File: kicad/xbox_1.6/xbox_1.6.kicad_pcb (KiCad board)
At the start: 2 copper layers, 6 parts, among them U2C1 intel_495_bga2, U4B1 ddr_100_tqfp, U4C1 nvidia_xgpu_nv2a, U5F1 ddr_100_tqfp, U6D1 ddr_100_tqfp, U6E1 nvidia_mcpx

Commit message: route more
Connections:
- U2C1 pad A2: (no net) -> /VSS
- U2C1 pad A3: (no net) -> /CPU_A29
- U2C1 pad A4: (no net) -> /CPU_A32
- U2C1 pad A5: (no net) -> /CPU_A33
- U2C1 pad A6: (no net) -> /CPU_RESET
- U2C1 pad A7: (no net) -> /VSS
- U2C1 pad A8: (no net) -> /VSS
- U2C1 pad A9: (no net) -> /CPU_D5
- U2C1 pad B1: (no net) -> /VSS
- U2C1 pad B2: (no net) -> /CPU_A30
- U2C1 pad B3: (no net) -> /CPU_A28
- U2C1 pad B4: (no net) -> /CPU_A34
- U2C1 pad B5: (no net) -> /VSS
- U2C1 pad B6: (no net) -> /VSS
- U2C1 pad B7: (no net) -> /VSS
- U2C1 pad B8: (no net) -> /VSS
- U2C1 pad C1: (no net) -> /CPU_A27
- U2C1 pad C2: (no net) -> /CPU_A31
- U2C1 pad C3: (no net) -> /CPU_A26
- U2C1 pad C4: (no net) -> /CPU_A20
- U2C1 pad C5: (no net) -> /CPU_A35
- U2C1 pad C6: (no net) -> /CPU_BREQ0
- U2C1 pad C7: (no net) -> /CPU_D2
- U2C1 pad C8: (no net) -> /CPU_D3
- U2C1 pad D1: (no net) -> /CPU_A22
- U2C1 pad D2: (no net) -> /VSS
- U2C1 pad D3: (no net) -> /CPU_A21
- U2C1 pad D4: (no net) -> /CPU_A25
- U2C1 pad D5: (no net) -> /CPU_A24
- U2C1 pad D6: (no net) -> /VSS
- U2C1 pad D7: (no net) -> /VSS
- U2C1 pad E1: (no net) -> /CPU_A19
- U2C1 pad E2: (no net) -> /CPU_A23
- U2C1 pad E3: (no net) -> /VSS
- U2C1 pad E4: (no net) -> /CPU_A15
- U2C1 pad E5: (no net) -> /CPU_VREF
- U2C1 pad E6: (no net) -> /CPU_BERR
- U2C1 pad F1: (no net) -> /CPU_A16
- U2C1 pad F2: (no net) -> /CPU_A18
- U2C1 pad F3: (no net) -> /VSS
- U2C1 pad F4: (no net) -> /CPU_A17
- U2C1 pad F5: (no net) -> /CPU_VREF
- U2C1 pad G1: (no net) -> /CPU_A13
- U2C1 pad G3: (no net) -> /VSS
- U2C1 pad G4: (no net) -> /CPU_G4_NC
- U2C1 pad H1: (no net) -> /CPU_A14
- U2C1 pad H2: (no net) -> /VSS
- U2C1 pad H4: (no net) -> /CPU_H4_NC
- U2C1 pad J1: (no net) -> /CPU_A10
- U2C1 pad J2: (no net) -> /CPU_A5
- U2C1 pad J3: (no net) -> /CPU_A11
- U2C1 pad J4: (no net) -> /VSS
- U2C1 pad K1: (no net) -> /CPU_A9
- U2C1 pad K2: (no net) -> /VSS
- U2C1 pad K3: (no net) -> /CPU_A4
- U2C1 pad K4: (no net) -> /CPU_A12
- U2C1 pad K5: (no net) -> /CPU_A8
- U2C1 pad L5: (no net) -> /VSS
- U4C1 pad A14: (no net) -> /CPU_D4
- U4C1 pad A16: (no net) -> /CPU_A27
- U4C1 pad A17: (no net) -> /CPU_A14
- U4C1 pad A18: (no net) -> /CPU_A10
- U4C1 pad A19: (no net) -> /CPU_A4
- U4C1 pad A20: (no net) -> /CPU_A8
- U4C1 pad B14: (no net) -> /CPU_D5
- U4C1 pad B16: (no net) -> /CPU_A29
- U4C1 pad B18: (no net) -> /CPU_A11
- U4C1 pad B20: (no net) -> /CPU_A9
- U4C1 pad C17: (no net) -> /CPU_A13
- U4C1 pad C19: (no net) -> /CPU_A12
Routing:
- net /CPU_D5: track 0.00 -> 75.8 mm, vias 0 -> 1
- net /CPU_A14: track 0.00 -> 75.8 mm, vias 0 -> 1
- net /CPU_A10: track 0.00 -> 75.7 mm, vias 0 -> 1
- net /CPU_D4: track 0.00 -> 75.7 mm, vias 0 -> 1
- net /CPU_A4: track 0.00 -> 75.7 mm, vias 0 -> 1
- net /CPU_A29: track 0.00 -> 75.5 mm, vias 0 -> 1
- net /CPU_A13: track 0.00 -> 75.5 mm, vias 0 -> 1
- net /CPU_A8: track 0.00 -> 75.4 mm, vias 0 -> 1
- net /CPU_A11: track 0.00 -> 74.5 mm, vias 0 -> 1
- net /CPU_A12: track 0.00 -> 73.9 mm, vias 0 -> 1
- net /CPU_A9: track 0.00 -> 72.7 mm, vias 0 -> 1
- net /CPU_A27: track 0.00 -> 71.4 mm, vias 0 -> 1
- net /VSS: track 46.2 -> 65.6 mm, vias 25 -> 41
- net /CPU_BREQ0: track 0.00 -> 11.0 mm, vias 0 -> 1
- net /CPU_VREF: track 3.05 -> 8.39 mm, vias 1 -> 3
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
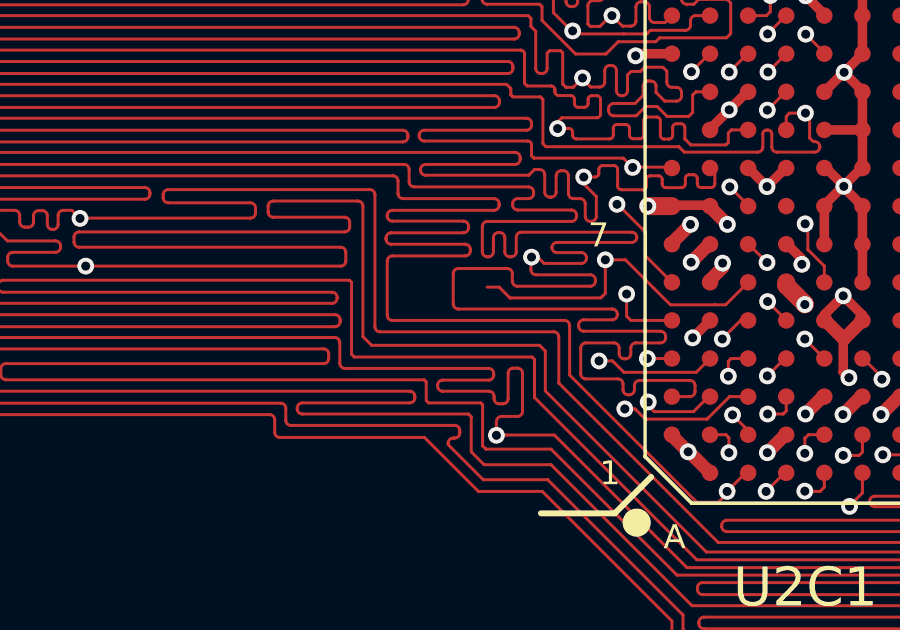
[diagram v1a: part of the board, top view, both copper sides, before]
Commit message: add 0603 footprint
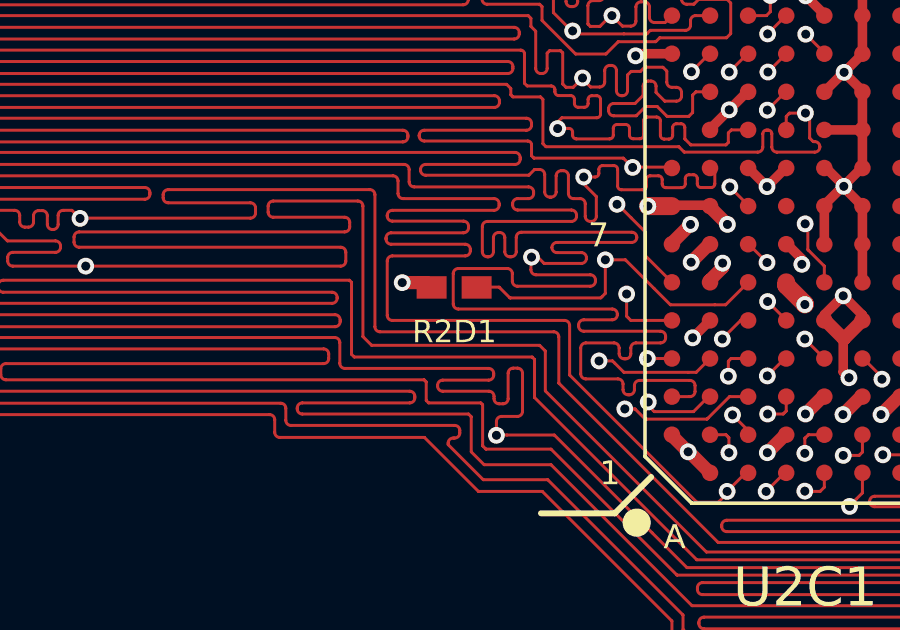
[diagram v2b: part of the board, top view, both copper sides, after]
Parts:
- added R2D1: 0603_smd, xbox_footprint:0603_smd, F.Cu at (253.3, 123.3)
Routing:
- net /VSS: track 65.6 -> 66.7 mm, vias 41 -> 42
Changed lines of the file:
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@@
     (pad "Y34" smd circle (at 16.5 2.5 270) (size 0.45 0.45) (layers "F.Cu" "F.Paste" "F.Mask"))
+  )
+  (footprint "xbox_footprint:0603_smd" (layer "F.Cu")
+    (at 253.28 123.28)
+    (attr smd)
+    (fp_text reference "R2D1" (at 0.01 1.48 unlocked) (layer "F.SilkS")
+        (effects (font (size 0.75 0.75) (thickness 0.15)))
+    )
+    (fp_text value "0603_smd" (at -0.01 4.12 unlocked) (layer "F.Fab")
+        (effects (font (size 1 1) (thickness 0.15)))
+    )
+    (fp_text user "10 Ohm" (at 0 2.75 unlocked) (layer "F.Fab")
+        (effects (font (size 1 1) (thickness 0.15)))
+    )
+    (fp_rect (start -1.295 -0.42) (end 1.295 0.42)
+      (stroke (width 0.05) (type default)) (fill none) (layer "F.CrtYd"))
+    (pad "1" smd rect (at -0.75 0) (size 1 0.75) (layers "F.Cu" "F.Paste" "F.Mask")
+      (net 4 "/VSS") (thermal_bridge_angle 45))
+    (pad "2" smd rect (at 0.75 0) (size 1 0.75) (layers "F.Cu" "F.Paste" "F.Mask")
+      (net 84 "/CPU_BREQ0") (thermal_bridge_angle 45))
   )
   (footprint "xbox_footprint:nvidia_mcpx" (layer "F.Cu")
@@
   (segment (start 264.35 121.84) (end 264.38 121.84) (width 0.32) (layer "F.Cu") (net 4))
   (segment (start 261.78 120.54) (end 261.81 120.57) (width 0.32) (layer "F.Cu") (net 4))
+  (segment (start 252.53 123.28) (end 252.37 123.12) (width 0.44) (layer "F.Cu") (net 4))
   (segment (start 266.27 119.89) (end 265.68 119.3) (width 0.32) (layer "F.Cu") (net 4))
   (segment (start 268.16 126.92) (end 268.11 126.92) (width 0.44) (layer "F.Cu") (net 4))
@@
   (segment (start 264.87 122.33) (end 264.87 122.51) (width 0.32) (layer "F.Cu") (net 4))
   (segment (start 275.8 105.31) (end 275.8 104.4) (width 0.44) (layer "F.Cu") (net 4))
+  (segment (start 252.37 123.12) (end 251.55 123.12) (width 0.44) (layer "F.Cu") (net 4))
   (segment (start 270.7 125.58) (end 270.7 125.65) (width 0.4) (layer "F.Cu") (net 4))
   (segment (start 263.05 116.76) (end 262.45 117.36) (width 0.32) (layer "F.Cu") (net 4))
@@
   (via (at 262.44 111.05) (size 0.56) (drill 0.3) (layers "F.Cu" "B.Cu") (net 4))
   (via (at 259.74 120.57) (size 0.56) (drill 0.3) (layers "F.Cu" "B.Cu") (net 4))
+  (via (at 251.55 123.12) (size 0.56) (drill 0.3) (layers "F.Cu" "B.Cu") (net 4))
   (via (at 264.97 123.85) (size 0.56) (drill 0.3) (layers "F.Cu" "B.Cu") (net 4))
   (via (at 275.16 107.26) (size 0.56) (drill 0.3) (layers "F.Cu" "B.Cu") (net 4))

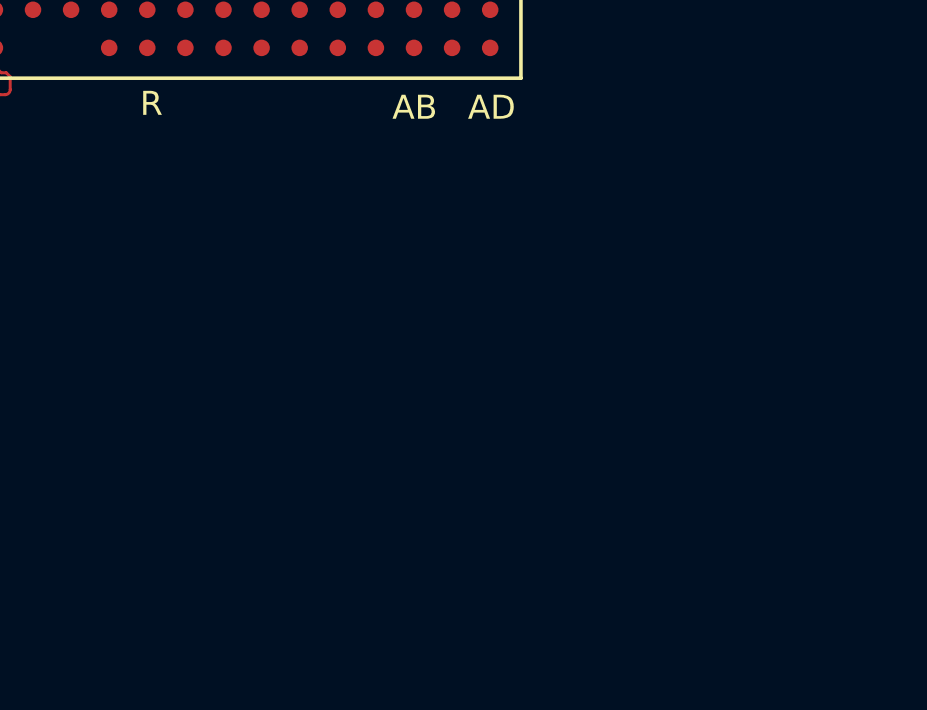
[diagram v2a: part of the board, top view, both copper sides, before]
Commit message: add some footprints
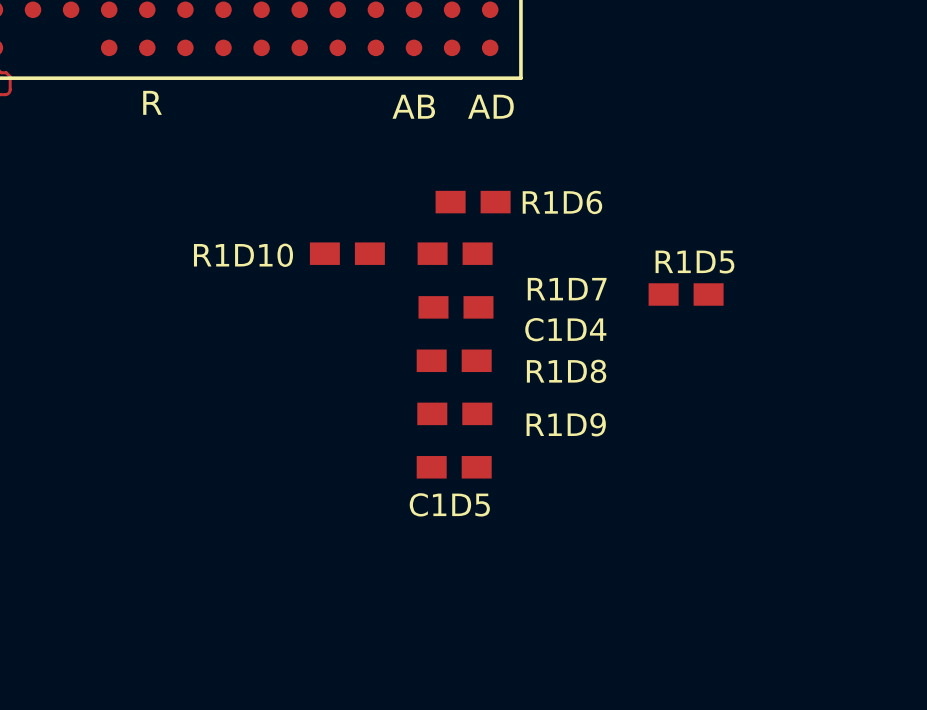
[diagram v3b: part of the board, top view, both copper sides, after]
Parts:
- added C1D4: 0603_smd, xbox_footprint:0603_smd, F.Cu at (288.6, 138.1)
- added C1D5: 0603_smd, xbox_footprint:0603_smd, F.Cu at (288.6, 143.4)
- added R1D10: 0603_smd, xbox_footprint:0603_smd, F.Cu at (285.0, 136.3)
- added R1D5: 0603_smd, xbox_footprint:0603_smd, F.Cu at (296.3, 137.7)
- added R1D6: 0603_smd, xbox_footprint:0603_smd, F.Cu at (289.2, 134.6)
- added R1D7: 0603_smd, xbox_footprint:0603_smd, F.Cu at (288.6, 136.3)
- added R1D8: 0603_smd, xbox_footprint:0603_smd, F.Cu at (288.6, 139.9)
- added R1D9: 0603_smd, xbox_footprint:0603_smd, F.Cu at (288.6, 141.7)
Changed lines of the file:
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@@
   (net 116 "/CPU_A8")
   (net 117 "/CPU_A9")
+  (footprint "xbox_footprint:0603_smd" (layer "F.Cu")
+    (at 288.58 136.32)
+    (attr smd)
+    (fp_text reference "R1D7" (at 3.73 1.21 unlocked) (layer "F.SilkS")
+        (effects (font (size 0.75 0.75) (thickness 0.15)))
+    )
+    (fp_text value "0603_smd" (at -0.01 4.12 unlocked) (layer "F.Fab")
+        (effects (font (size 1 1) (thickness 0.15)))
+    )
+    (fp_text user "${REFERENCE}" (at 0 2.75 unlocked) (layer "F.Fab")
+        (effects (font (size 1 1) (thickness 0.15)))
+    )
+    (fp_rect (start -1.295 -0.42) (end 1.295 0.42)
+      (stroke (width 0.05) (type default)) (fill none) (layer "F.CrtYd"))
+    (pad "1" smd rect (at -0.75 0) (size 1 0.75) (layers "F.Cu" "F.Paste" "F.Mask")
+      (thermal_bridge_angle 45))
+    (pad "2" smd rect (at 0.75 0) (size 1 0.75) (layers "F.Cu" "F.Paste" "F.Mask")
+      (thermal_bridge_angle 45))
+  )
+  (footprint "xbox_footprint:0603_smd" (layer "F.Cu")
+    (at 288.57 141.66)
+    (attr smd)
+    (fp_text reference "R1D9" (at 3.7 0.39 unlocked) (layer "F.SilkS")
+        (effects (font (size 0.75 0.75) (thickness 0.15)))
+    )
+    (fp_text value "0603_smd" (at -0.01 4.12 unlocked) (layer "F.Fab")
+        (effects (font (size 1 1) (thickness 0.15)))
+    )
+    (fp_text user "${REFERENCE}" (at 0 2.75 unlocked) (layer "F.Fab")
+        (effects (font (size 1 1) (thickness 0.15)))
+    )
+    (fp_rect (start -1.295 -0.42) (end 1.295 0.42)
+      (stroke (width 0.05) (type default)) (fill none) (layer "F.CrtYd"))
+    (pad "1" smd rect (at -0.75 0) (size 1 0.75) (layers "F.Cu" "F.Paste" "F.Mask")
+      (thermal_bridge_angle 45))
+    (pad "2" smd rect (at 0.75 0) (size 1 0.75) (layers "F.Cu" "F.Paste" "F.Mask")
+      (thermal_bridge_angle 45))
+  )
   (footprint "xbox_footprint:intel_495_bga2" (layer "F.Cu")
     (at 275.145 116.76)
@@
   )
   (footprint "xbox_footprint:0603_smd" (layer "F.Cu")
+    (at 288.55 139.89)
+    (attr smd)
+    (fp_text reference "R1D8" (at 3.73 0.38 unlocked) (layer "F.SilkS")
+        (effects (font (size 0.75 0.75) (thickness 0.15)))
+    )
+    (fp_text value "0603_smd" (at -0.01 4.12 unlocked) (layer "F.Fab")
+        (effects (font (size 1 1) (thickness 0.15)))
+    )
+    (fp_text user "${REFERENCE}" (at 0 2.75 unlocked) (layer "F.Fab")
+        (effects (font (size 1 1) (thickness 0.15)))
+    )
+    (fp_rect (start -1.295 -0.42) (end 1.295 0.42)
+      (stroke (width 0.05) (type default)) (fill none) (layer "F.CrtYd"))
+    (pad "1" smd rect (at -0.75 0) (size 1 0.75) (layers "F.Cu" "F.Paste" "F.Mask")
+      (thermal_bridge_angle 45))
+    (pad "2" smd rect (at 0.75 0) (size 1 0.75) (layers "F.Cu" "F.Paste" "F.Mask")
+      (thermal_bridge_angle 45))
+  )
+  (footprint "xbox_footprint:0603_smd" (layer "F.Cu")
     (at 253.28 123.28)
     (attr smd)
@@
     (pad "2" smd rect (at 0.75 0) (size 1 0.75) (layers "F.Cu" "F.Paste" "F.Mask")
       (net 84 "/CPU_BREQ0") (thermal_bridge_angle 45))
+  )
+  (footprint "xbox_footprint:0603_smd" (layer "F.Cu")
+    (at 296.28 137.68)
+    (attr smd)
+    (fp_text reference "R1D5" (at 0.29 -1.06 unlocked) (layer "F.SilkS")
+        (effects (font (size 0.75 0.75) (thickness 0.15)))
+    )
+    (fp_text value "0603_smd" (at -0.01 4.12 unlocked) (layer "F.Fab")
+        (effects (font (size 1 1) (thickness 0.15)))
+    )
+    (fp_text user "${REFERENCE}" (at 0 2.75 unlocked) (layer "F.Fab")
+        (effects (font (size 1 1) (thickness 0.15)))
+    )
+    (fp_rect (start -1.295 -0.42) (end 1.295 0.42)
+      (stroke (width 0.05) (type default)) (fill none) (layer "F.CrtYd"))
+    (pad "1" smd rect (at -0.75 0) (size 1 0.75) (layers "F.Cu" "F.Paste" "F.Mask")
+      (thermal_bridge_angle 45))
+    (pad "2" smd rect (at 0.75 0) (size 1 0.75) (layers "F.Cu" "F.Paste" "F.Mask")
+      (thermal_bridge_angle 45))
+  )
+  (footprint "xbox_footprint:0603_smd" (layer "F.Cu")
+    (at 288.55 143.44)
+    (attr smd)
+    (fp_text reference "C1D5" (at -0.13 1.28 unlocked) (layer "F.SilkS")
+        (effects (font (size 0.75 0.75) (thickness 0.15)))
+    )
+    (fp_text value "0603_smd" (at -0.01 4.12 unlocked) (layer "F.Fab")
+        (effects (font (size 1 1) (thickness 0.15)))
+    )
+    (fp_text user "${REFERENCE}" (at 0 2.75 unlocked) (layer "F.Fab")
+        (effects (font (size 1 1) (thickness 0.15)))
+    )
+    (fp_rect (start -1.295 -0.42) (end 1.295 0.42)
+      (stroke (width 0.05) (type default)) (fill none) (layer "F.CrtYd"))
+    (pad "1" smd rect (at -0.75 0) (size 1 0.75) (layers "F.Cu" "F.Paste" "F.Mask")
+      (thermal_bridge_angle 45))
+    (pad "2" smd rect (at 0.75 0) (size 1 0.75) (layers "F.Cu" "F.Paste" "F.Mask")
+      (thermal_bridge_angle 45))
+  )
+  (footprint "xbox_footprint:0603_smd" (layer "F.Cu")
+    (at 289.18 134.6)
+    (attr smd)
+    (fp_text reference "R1D6" (at 2.96 0.04 unlocked) (layer "F.SilkS")
+        (effects (font (size 0.75 0.75) (thickness 0.15)))
+    )
+    (fp_text value "0603_smd" (at -0.01 4.12 unlocked) (layer "F.Fab")
+        (effects (font (size 1 1) (thickness 0.15)))
+    )
+    (fp_text user "${REFERENCE}" (at 0 2.75 unlocked) (layer "F.Fab")
+        (effects (font (size 1 1) (thickness 0.15)))
+    )
+    (fp_rect (start -1.295 -0.42) (end 1.295 0.42)
+      (stroke (width 0.05) (type default)) (fill none) (layer "F.CrtYd"))
+    (pad "1" smd rect (at -0.75 0) (size 1 0.75) (layers "F.Cu" "F.Paste" "F.Mask")
+      (thermal_bridge_angle 45))
+    (pad "2" smd rect (at 0.75 0) (size 1 0.75) (layers "F.Cu" "F.Paste" "F.Mask")
+      (thermal_bridge_angle 45))
   )
   (footprint "xbox_footprint:nvidia_mcpx" (layer "F.Cu")
@@
     (pad "Y22" smd circle (at 10.5 8.5 180) (size 0.45 0.45) (layers "F.Cu" "F.Paste" "F.Mask"))
   )
+  (footprint "xbox_footprint:0603_smd" (layer "F.Cu")
+    (at 284.99 136.32)
+    (attr smd)
+    (fp_text reference "R1D10" (at -3.48 0.08 unlocked) (layer "F.SilkS")
+        (effects (font (size 0.75 0.75) (thickness 0.15)))
+    )
+    (fp_text value "0603_smd" (at -0.01 4.12 unlocked) (layer "F.Fab")
+        (effects (font (size 1 1) (thickness 0.15)))
+    )
+    (fp_text user "${REFERENCE}" (at 0 2.75 unlocked) (layer "F.Fab")
+        (effects (font (size 1 1) (thickness 0.15)))
+    )
+    (fp_rect (start -1.295 -0.42) (end 1.295 0.42)
+      (stroke (width 0.05) (type default)) (fill none) (layer "F.CrtYd"))
+    (pad "1" smd rect (at -0.75 0) (size 1 0.75) (layers "F.Cu" "F.Paste" "F.Mask")
+      (thermal_bridge_angle 45))
+    (pad "2" smd rect (at 0.75 0) (size 1 0.75) (layers "F.Cu" "F.Paste" "F.Mask")
+      (thermal_bridge_angle 45))
+  )
   (footprint "xbox_footprint:ddr_100_tqfp" (layer "F.Cu")
     (at 162.18 127.88 -90)
@@
       (thermal_bridge_angle 45))
   )
+  (footprint "xbox_footprint:0603_smd" (layer "F.Cu")
+    (at 288.61 138.11)
+    (attr smd)
+    (fp_text reference "C1D4" (at 3.66 0.77 unlocked) (layer "F.SilkS")
+        (effects (font (size 0.75 0.75) (thickness 0.15)))
+    )
+    (fp_text value "0603_smd" (at -0.01 4.12 unlocked) (layer "F.Fab")
+        (effects (font (size 1 1) (thickness 0.15)))
+    )
+    (fp_text user "${REFERENCE}" (at 0 2.75 unlocked) (layer "F.Fab")
+        (effects (font (size 1 1) (thickness 0.15)))
+    )
+    (fp_rect (start -1.295 -0.42) (end 1.295 0.42)
+      (stroke (width 0.05) (type default)) (fill none) (layer "F.CrtYd"))
+    (pad "1" smd rect (at -0.75 0) (size 1 0.75) (layers "F.Cu" "F.Paste" "F.Mask")
+      (thermal_bridge_angle 45))
+    (pad "2" smd rect (at 0.75 0) (size 1 0.75) (layers "F.Cu" "F.Paste" "F.Mask")
+      (thermal_bridge_angle 45))
+  )

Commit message: route more
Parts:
- added R1D2: 0603_smd, xbox_footprint:0603_smd, F.Cu at (299.4, 125.3)
- added R1D3: 0603_smd, xbox_footprint:0603_smd, F.Cu at (299.5, 127.1)
- added R1D4: 0603_smd, xbox_footprint:0603_smd, F.Cu at (299.4, 128.9)
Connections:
- U2C1 pad L1: (no net) -> /CPU_A7
- U2C1 pad L2: (no net) -> /CPU_PLL1
- U2C1 pad L3: (no net) -> /CPU_A3
- U2C1 pad L4: (no net) -> /CPU_A6
- U2C1 pad M2: (no net) -> /CPU_PLL2
- U2C1 pad M3: (no net) -> /CPU_BCLK
- U2C1 pad M4: (no net) -> /CPU_M4_NC
- U2C1 pad N2: (no net) -> /VSS
- U2C1 pad N3: (no net) -> /VSS
- U2C1 pad N4: (no net) -> /VSS
- U2C1 pad N5: (no net) -> /CPU_TESTLO2
- U2C1 pad N6: (no net) -> /CPU_VCCT
- U2C1 pad P1: (no net) -> /VSS
- U2C1 pad P2: (no net) -> /CPU_CLKREF
- U2C1 pad P5: (no net) -> /VSS
- U2C1 pad R1: (no net) -> /CPU_LOCK
- U2C1 pad R3: (no net) -> /VSS
- U2C1 pad R4: (no net) -> /VSS
- U2C1 pad R5: (no net) -> /VSS
- U2C1 pad T1: (no net) -> /CPU_DRDY
- U2C1 pad T2: (no net) -> /CPU_REQ0
- U2C1 pad T3: (no net) -> /VSS
- U2C1 pad T4: (no net) -> /CPU_BNR
- U2C1 pad T5: (no net) -> /VSS
- U2C1 pad U1: (no net) -> /CPU_RS0
- U2C1 pad U2: (no net) -> /CPU_TRDY
- U2C1 pad U3: (no net) -> /CPU_DEFER
- U2C1 pad U4: (no net) -> /CPU_BPRI
- U2C1 pad U5: (no net) -> /CPU_VREF
- U2C1 pad V3: (no net) -> /VSS
- U4C1 pad A22: (no net) -> /CPU_A6
- U4C1 pad A23: (no net) -> /CPU_RS0
- U4C1 pad A24: (no net) -> /CPU_DEFER
- U4C1 pad B22: (no net) -> /CPU_A3
- U4C1 pad C21: (no net) -> /CPU_A7
- U4C1 pad C23: (no net) -> /CPU_BNR
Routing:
- net /CPU_RS0: track 0.00 -> 76.5 mm, vias 0 -> 1
- net /CPU_A7: track 0.00 -> 76.2 mm, vias 0 -> 1
- net /CPU_A3: track 0.00 -> 76.1 mm, vias 0 -> 1
- net /CPU_BNR: track 0.00 -> 75.9 mm, vias 0 -> 1
- net /CPU_A6: track 0.00 -> 74.6 mm, vias 0 -> 1
- net /CPU_DEFER: track 0.00 -> 70.2 mm, vias 0 -> 1
- net /CPU_VREF: track 8.39 -> 30.9 mm, vias 3 -> 6
- net /CPU_BPRI: track 0.00 -> 18.3 mm, vias 0 -> 1
- net /CPU_BCLK: track 0.00 -> 17.5 mm, vias 0 -> 1
- net /CPU_TRDY: track 0.00 -> 15.6 mm, vias 0 -> 1
- net /CPU_REQ0: track 0.00 -> 15.0 mm, vias 0 -> 1
- net /CPU_LOCK: track 0.00 -> 14.1 mm, vias 0 -> 1
- net /CPU_DRDY: track 0.00 -> 13.9 mm, vias 0 -> 1
- net /VSS: track 66.7 -> 79.5 mm, vias 42 -> 47
- net /CPU_TESTLO2: track 0.00 -> 3.33 mm, vias 0 -> 1
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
